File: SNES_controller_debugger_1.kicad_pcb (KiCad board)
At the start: 2 copper layers, 100 x 74 mm, 22 parts, among them J1 ICSP, J2 CONTROLLER_OUT, J3 MICRO_USB, SW1 Reset, U1 ATmega32U4, Y1 16MHz

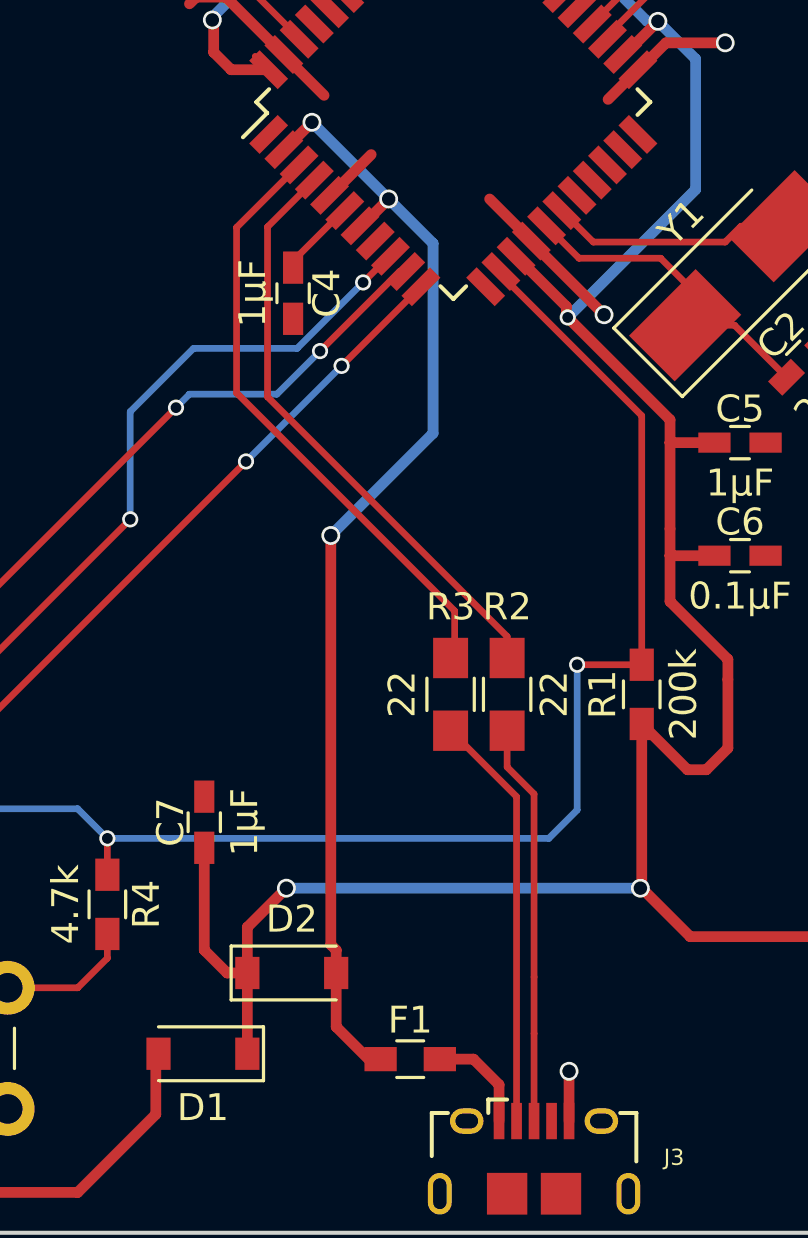
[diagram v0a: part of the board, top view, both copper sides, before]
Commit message: pcb: Tweak USB traces, fill an area with a ground plane.
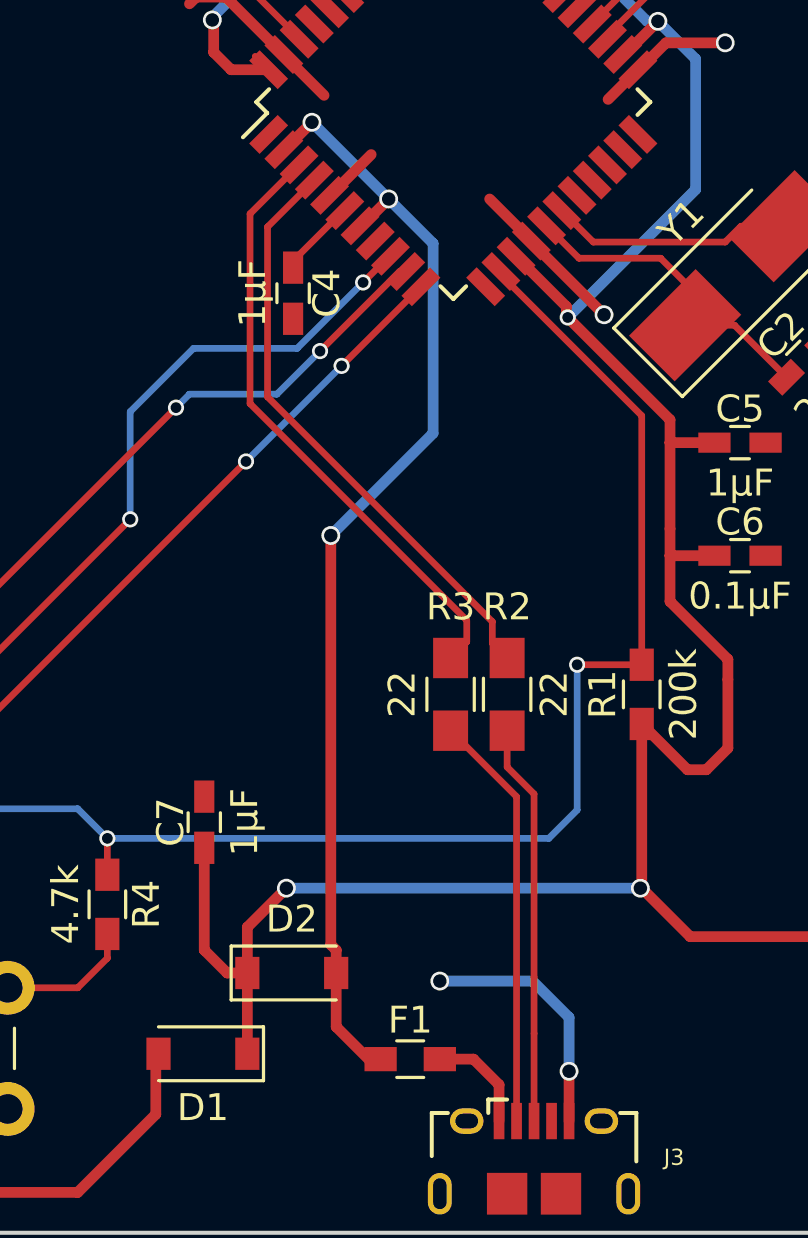
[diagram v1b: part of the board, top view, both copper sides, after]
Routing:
- net Earth: track 31.7 -> 39.1 mm, vias 4 -> 5
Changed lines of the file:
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@@
-(kicad_pcb (version 4) (host pcbnew 4.0.6-e0-6349~53~ubuntu16.04.1)
+(kicad_pcb (version 4) (host pcbnew 4.0.7-e1-6374~58~ubuntu16.04.1)
   (general
     (links 69)
@@
     (thickness 1.6)
     (drawings 5)
-    (tracks 315)
+    (tracks 322)
     (zones 0)
     (modules 22)
@@
     (42 Eco1.User user hide)
     (43 Eco2.User user hide)
-    (44 Edge.Cuts user hide)
+    (44 Edge.Cuts user)
     (45 Margin user hide)
     (46 B.CrtYd user hide)
-    (47 F.CrtYd user)
+    (47 F.CrtYd user hide)
     (48 B.Fab user hide)
     (49 F.Fab user hide)
@@
   (segment (start 121.272435 116.622435) (end 118.721751 114.071751) (width 0.25) (layer F.Cu) (net 1))
   (segment (start 121.166548 116.666548) (end 121.272435 116.666548) (width 0.25) (layer F.Cu) (net 1))
+  (via (at 126.5 151.65) (size 0.7) (drill 0.5) (layers F.Cu B.Cu) (net 2))
+  (segment (start 129.95 151.65) (end 126.5 151.65) (width 0.4) (layer B.Cu) (net 2))
+  (segment (start 131.3 153) (end 129.95 151.65) (width 0.4) (layer B.Cu) (net 2))
+  (segment (start 131.3 155) (end 131.3 153) (width 0.4) (layer B.Cu) (net 2))
+  (via (at 131.3 155) (size 0.7) (drill 0.5) (layers F.Cu B.Cu) (net 2))
+  (segment (start 131.3 156.85) (end 131.3 155) (width 0.4) (layer F.Cu) (net 2))
   (segment (start 133.858936 117.797918) (end 133.852082 117.797918) (width 0.4) (layer F.Cu) (net 2))
   (segment (start 133.852082 117.797918) (end 132.75 118.9) (width 0.4) (layer F.Cu) (net 2))
@@
   (segment (start 120.70675 117.232233) (end 120.632233 117.232233) (width 0.25) (layer F.Cu) (net 2))
   (segment (start 129.899138 124.16188) (end 129.96188 124.16188) (width 0.25) (layer F.Cu) (net 2))
-  (segment (start 131.3 156.85) (end 131.3 155) (width 0.4) (layer F.Cu) (net 2))
-  (via (at 131.3 155) (size 0.7) (drill 0.5) (layers F.Cu B.Cu) (net 2))
   (segment (start 125.232233 112.70675) (end 125.20675 112.70675) (width 0.25) (layer F.Cu) (net 2))
   (segment (start 122.403806 122.464823) (end 122.403806 122.496194) (width 0.25) (layer F.Cu) (net 2))
@@
   (segment (start 130 151.5) (end 130 144.7) (width 0.25) (layer F.Cu) (net 23))
   (segment (start 130 144.7) (end 129 143.7) (width 0.25) (layer F.Cu) (net 23))
-  (segment (start 129 139.65) (end 129 138.85) (width 0.25) (layer F.Cu) (net 24))
-  (segment (start 120.1 123.637258) (end 121.83812 121.899138) (width 0.25) (layer F.Cu) (net 24))
+  (segment (start 120.1 129.95) (end 128.45 138.3) (width 0.25) (layer F.Cu) (net 24))
+  (segment (start 121.83812 121.899138) (end 120.1 123.637258) (width 0.25) (layer F.Cu) (net 24))
   (segment (start 120.1 129.95) (end 120.1 123.637258) (width 0.25) (layer F.Cu) (net 24))
-  (segment (start 129 138.85) (end 120.1 129.95) (width 0.25) (layer F.Cu) (net 24))
+  (segment (start 128.45 138.3) (end 128.45 139.1) (width 0.25) (layer F.Cu) (net 24))
+  (segment (start 128.45 139.1) (end 129 139.65) (width 0.25) (layer F.Cu) (net 24))
   (segment (start 121.83812 121.96188) (end 121.83812 121.899138) (width 0.25) (layer F.Cu) (net 24))
-  (segment (start 118.95 129.8) (end 127.05 137.9) (width 0.25) (layer F.Cu) (net 25))
-  (segment (start 118.95 129.8) (end 118.95 123.655887) (width 0.25) (layer F.Cu) (net 25))
-  (segment (start 121.272435 121.333452) (end 118.95 123.655887) (width 0.25) (layer F.Cu) (net 25))
-  (segment (start 127.05 137.9) (end 127.05 139.5) (width 0.25) (layer F.Cu) (net 25))
+  (segment (start 121.272435 121.333452) (end 121.266548 121.333452) (width 0.25) (layer F.Cu) (net 25))
+  (segment (start 121.266548 121.333452) (end 119.45 123.15) (width 0.25) (layer F.Cu) (net 25))
+  (segment (start 119.45 123.15) (end 119.45 130.2) (width 0.25) (layer F.Cu) (net 25))
+  (segment (start 119.45 130.2) (end 127.5 138.25) (width 0.25) (layer F.Cu) (net 25))
+  (segment (start 127.5 138.25) (end 127.5 139.05) (width 0.25) (layer F.Cu) (net 25))
+  (segment (start 127.5 139.05) (end 126.9 139.65) (width 0.25) (layer F.Cu) (net 25))
   (segment (start 127.05 139.5) (end 126.9 139.65) (width 0.25) (layer F.Cu) (net 25))
   (segment (start 120.8 148.2) (end 133.95 148.2) (width 0.4) (layer B.Cu) (net 26))

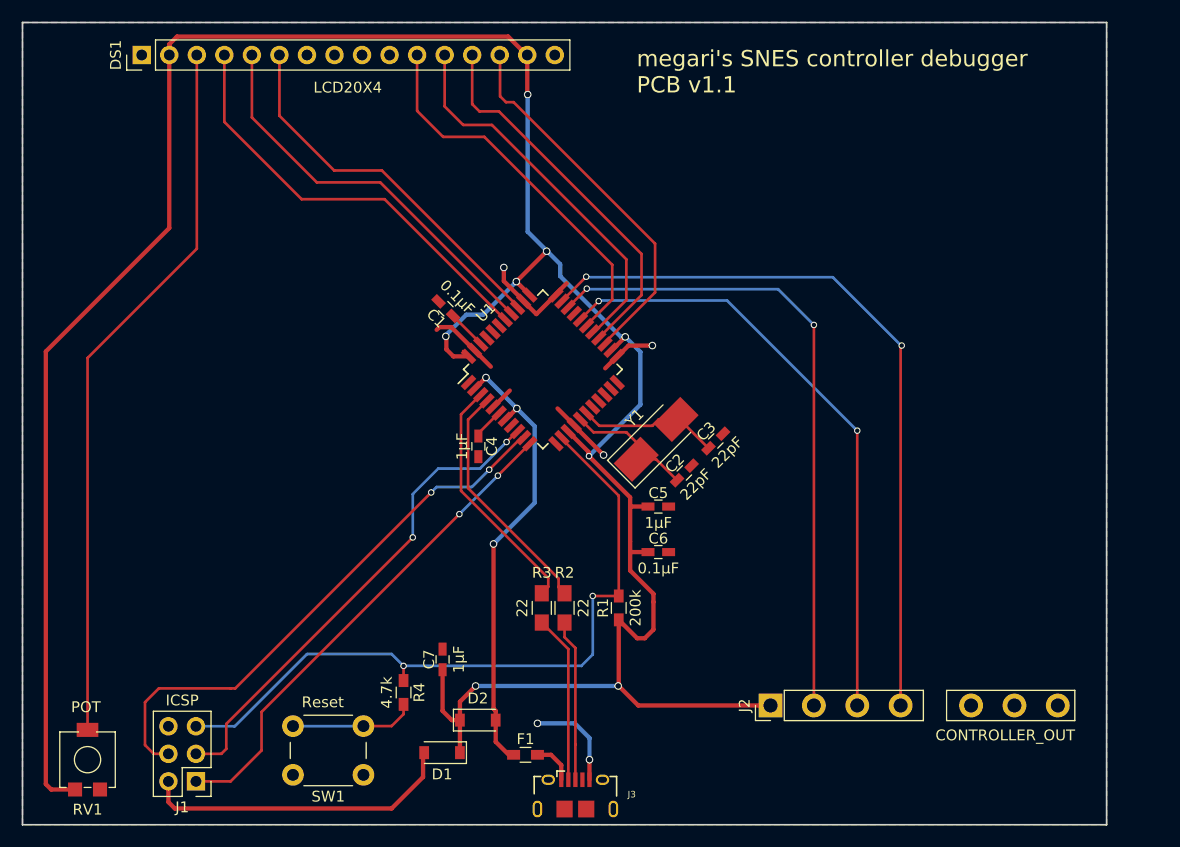
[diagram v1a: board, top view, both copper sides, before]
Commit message: pcb: Complete overhaul after getting some advice from an actual electronics engineer.
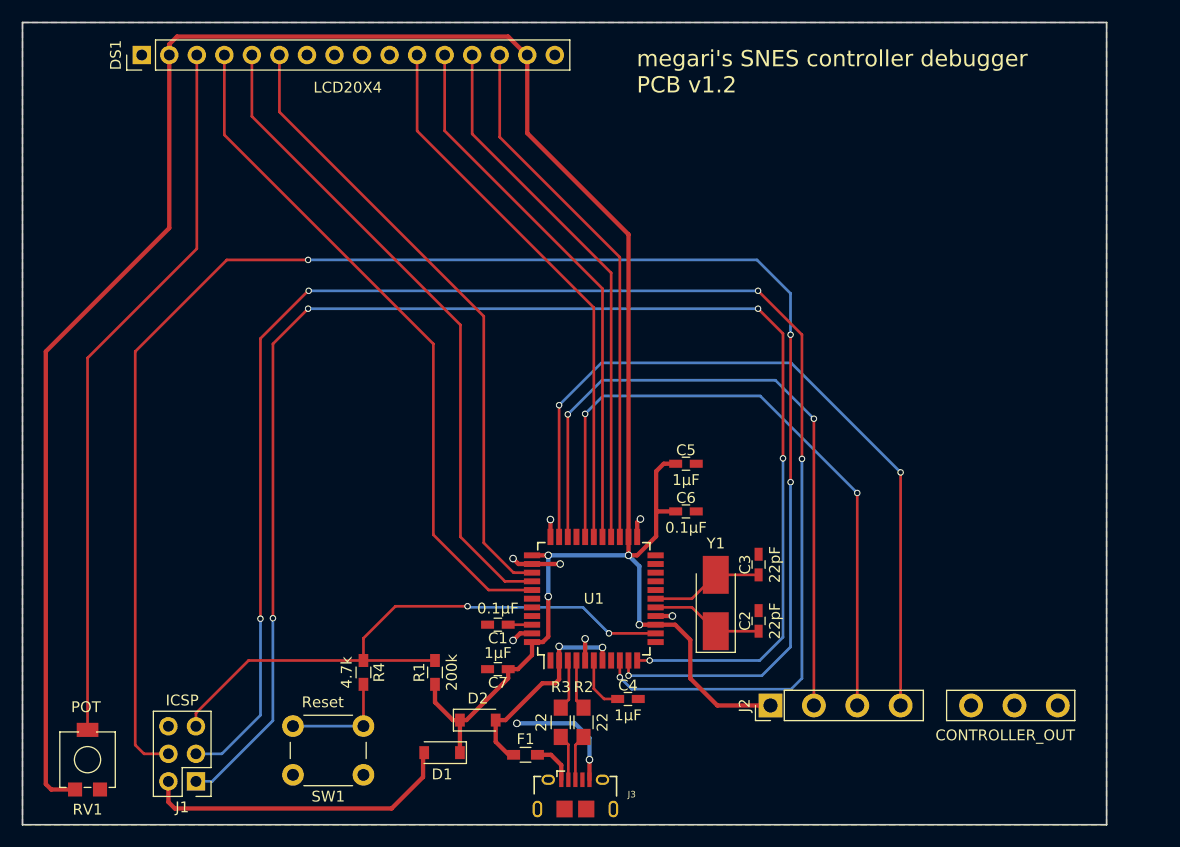
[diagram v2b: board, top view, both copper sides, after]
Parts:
- moved C1 29.5 mm to (122.8, 142.6), turned to 180 degrees
- moved C4 27.1 mm to (134.8, 149.4), turned to 0 degrees
- moved U1 21.7 mm to (131.7, 140.2), turned to 90 degrees
- moved R1 18.0 mm to (117.0, 146.9)
- moved Y1 16.1 mm to (142.9, 140.6), turned to 90 degrees
- moved C2 15.3 mm to (146.9, 142.2), turned to 90 degrees
- moved C3 12.1 mm to (146.9, 137.0), turned to 90 degrees
- moved R2 10.7 mm to (130.8, 151.6)
- moved R3 10.7 mm to (128.7, 151.6)
- moved C7 5.18 mm to (122.8, 146.7), turned to 180 degrees
- moved C5 4.70 mm to (140.2, 127.7)
- moved C6 4.53 mm to (140.2, 132.1)
- moved R4 4.14 mm to (110.5, 146.9)
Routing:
- net MOSI: track 51.5 -> 155.0 mm, vias 2 -> 4
- net SCLK: track 45.7 -> 146.5 mm, vias 2 -> 5
- net MISO: track 45.8 -> 135.9 mm, vias 2 -> 5
- net LCD_RS: track 39.6 -> 63.4 mm
- net LCD_RW: track 37.2 -> 60.7 mm
- net LCD_E: track 34.9 -> 58.4 mm
- net UVCC: track 42.4 -> 19.8 mm, vias 3 -> 2
- net D-: track 22.9 -> 4.70 mm
- net D+: track 22.2 -> 4.62 mm
- net VCC: track 250.7 -> 234.9 mm, vias 8 -> 4
- net LCD_D4: track 35.6 -> 51.2 mm
- net LCD_D5: track 35.4 -> 50.5 mm
- net LCD_D6: track 35.3 -> 49.8 mm
- net Earth: track 39.1 -> 24.6 mm, vias 5 -> 9
- net LCD_D7: track 34.9 -> 49.1 mm
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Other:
- board text added: "megari's SNES controller debugger PCB v1.2"
- board text removed: "megari's SNES controller debugger PCB v1.1"
